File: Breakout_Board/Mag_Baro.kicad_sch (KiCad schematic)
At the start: 2 parts, among them U4 MMC5983MA, U5 BMP581

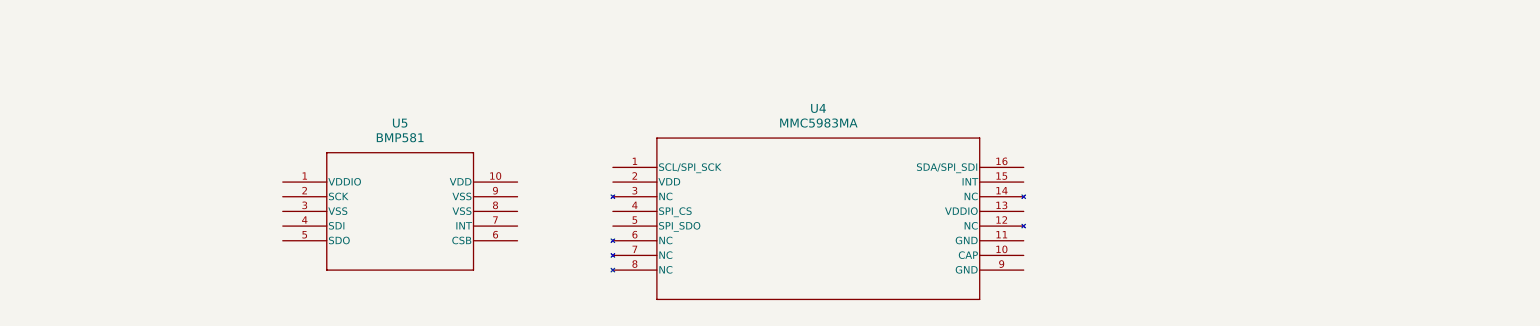
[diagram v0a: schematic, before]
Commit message: completed mag and baromet
fInished mag and barometer connections and connected to stm32f411, I just need the breakout pins to be done now.
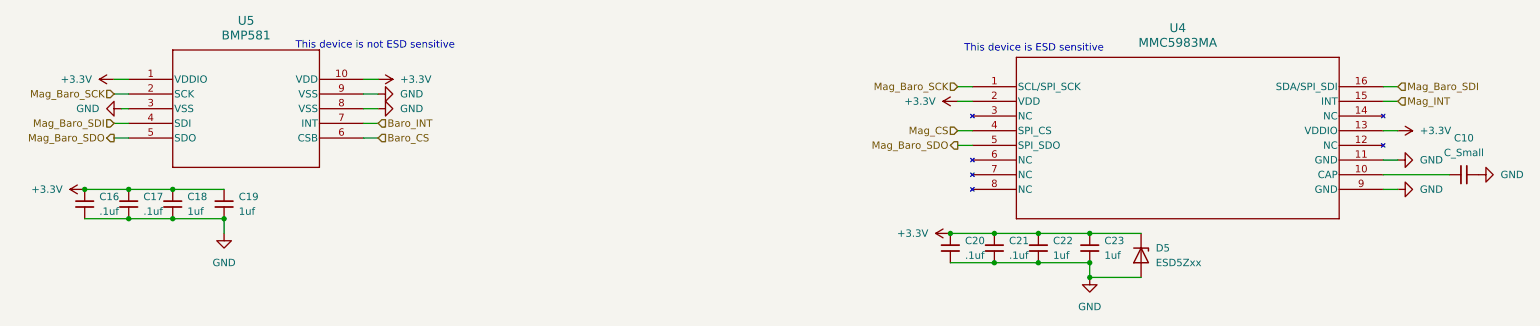
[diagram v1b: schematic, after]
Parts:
- added C10: C_Small, Package_LGA:Bosch_LGA-14_3x2.5mm_P0.5mm, symbol Device:C_Small
- added C16, C17, C20, C21: .1uf, Capacitor_SMD:C_0805_2012Metric_Pad1.18x1.45mm_HandSolder, symbol Device:C_Small
- added C18, C19, C22, C23: 1uf, Capacitor_SMD:C_0805_2012Metric_Pad1.18x1.45mm_HandSolder, symbol Device:C_Small
- added D5: ESD5Zxx, Diode_SMD:D_SOD-523, symbol Diode:ESD5Zxx
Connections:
- net +3.3V: now reaches U5.1 (VDDIO)
- net +3.3V: now also U4.13 (VDDIO), U4.2 (VDD), U5.10 (VDD), C16.1, C17.1, C18.1, C19.1, C20.1, C21.1, C22.1, C23.1, D5.1 (K)
- net Mag_Baro_SCK: now reaches U5.2 (SCK)
- net Mag_Baro_SCK: now also U4.1 (SCL/SPI_SCK)
- net GND: now reaches U5.3 (VSS)
- net GND: now also U4.11 (GND), U4.9 (GND), U5.8 (VSS), U5.9 (VSS), C10.2, C16.2, C17.2, C18.2, C19.2, C20.2, C21.2, C22.2, C23.2, D5.2 (A)
- net Mag_Baro_SDI: now reaches U5.4 (SDI)
- net Mag_Baro_SDI: now also U4.16 (SDA/SPI_SDI)
- net Mag_Baro_SDO: now reaches U5.5 (SDO)
- net Mag_Baro_SDO: now also U4.5 (SPI_SDO)
- net Baro_CS: now reaches U5.6 (CSB)
- net Baro_INT: now reaches U5.7 (INT)
- net at U4.10 (CAP): now also C10.1
- net Mag_INT: now reaches U4.15 (INT)
- net Mag_CS: now reaches U4.4 (SPI_CS)
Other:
- note added: "This device is ESD sensitive"
- note added: "This device is not ESD sensitive"
- moved on the sheet: U4, U5

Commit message: ready for breakout
Fixed up some work, now its ready for breakouts before final PCB layout
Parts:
- C10: value C_Small -> 10uf; footprint Package_LGA:Bosch_LGA-14_3x2.5mm_P0.5mm -> Capacitor_SMD:C_0805_2012Metric_Pad1.18x1.45mm_HandSolder
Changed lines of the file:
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@@
 			)
 		)
-		(property "Value" "C_Small"
+		(property "Value" "10uf"
 			(at 261.62 45.72 90)
 			(show_name no)
@@
 			)
 		)
-		(property "Footprint" "Package_LGA:Bosch_LGA-14_3x2.5mm_P0.5mm"
+		(property "Footprint" "Capacitor_SMD:C_0805_2012Metric_Pad1.18x1.45mm_HandSolder"
 			(at 261.62 49.53 0)
 			(hide yes)

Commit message: ready for routing
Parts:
- removed C17, C21: .1uf, Capacitor_SMD:C_0805_2012Metric_Pad1.18x1.45mm_HandSolder, symbol Device:C_Small
- removed C19, C23: 1uf, Capacitor_SMD:C_0805_2012Metric_Pad1.18x1.45mm_HandSolder, symbol Device:C_Small
